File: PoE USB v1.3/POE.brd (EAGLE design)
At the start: 70.6 x 58.3 mm, 20 parts, among them X1 RJ45-6L21-B, X2 RJ45-6L21-B

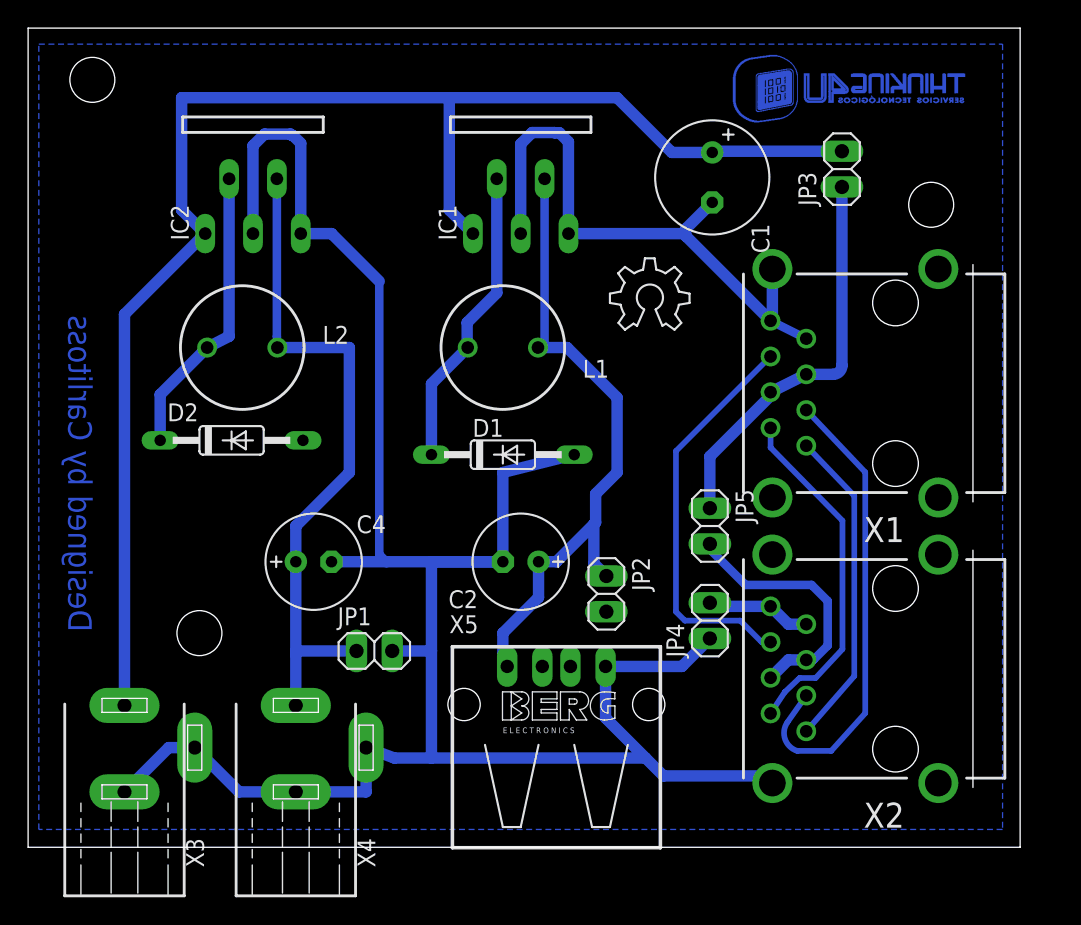
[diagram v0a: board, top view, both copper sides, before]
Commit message: PoE Modular acabado
Acabada la extracción o inyección de Power
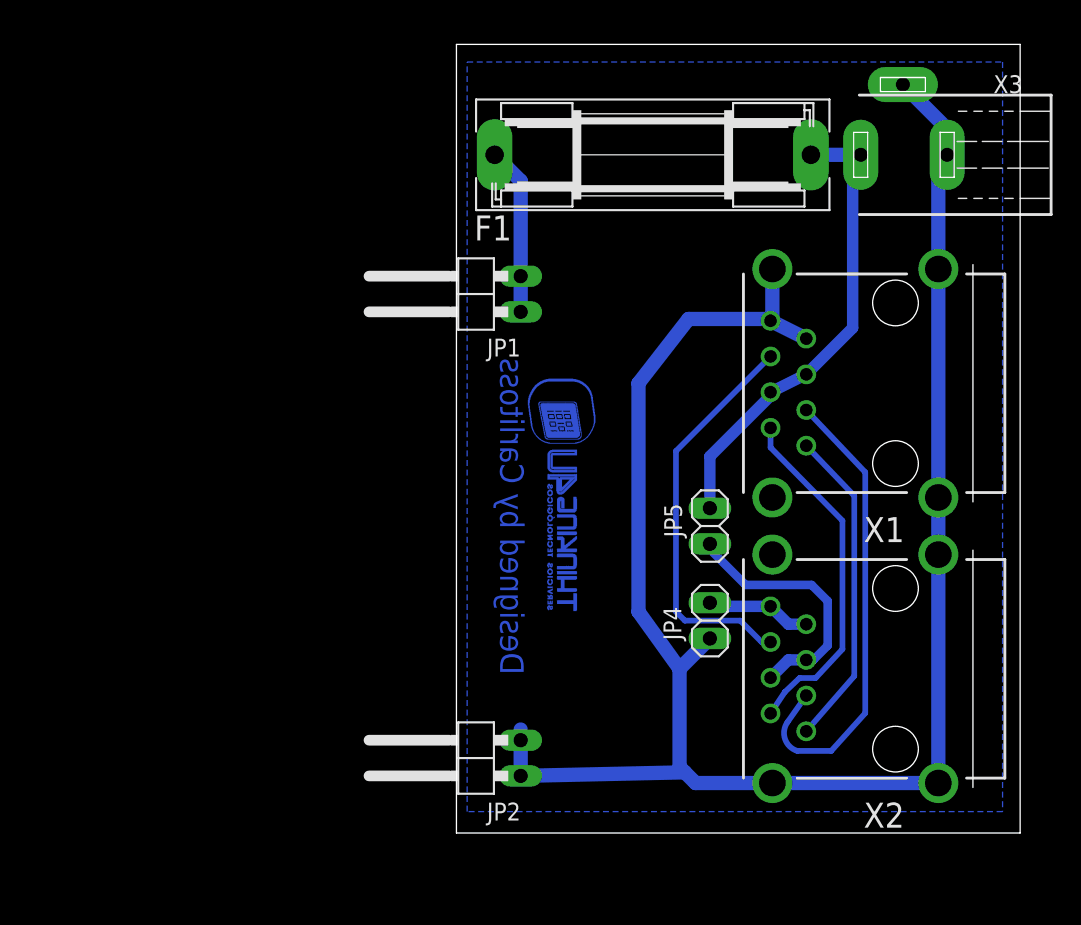
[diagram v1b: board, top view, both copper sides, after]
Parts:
- removed C1: 470uF, rcl:E3,5-8
- removed C2, C4: 220uF, rcl:E2,5-7
- removed D1, D2: 1N5824, diode:DO35-10
- removed IC1, IC2: (no value), linear:TO220-51
- removed JP3: (no value), pinhead:1X02
- removed L1, L2: 33uH, rcl:6000-XXXX-RC
- removed LOGO1: OSHW_LOGO_6MILX0200-NT, ohw-logo:OSHW_6X200_NOTEXT
- removed X4: (no value), con-conrad:733980-62
- removed X5: (no value), con-berg:PN87520
- added F1: (no value), fuse:SH22,5
- JP1, JP2: device pinhead:1X02 -> pinhead:1X02/90
- moved X3 77.4 mm to (158.5, 102.6), turned to 90 degrees
- moved JP1 26.2 mm to (121.9, 92.7), turned to 90 degrees
- moved JP2 15.3 mm to (121.9, 59.7), turned to 90 degrees
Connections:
- removed net N$2: C2.+, IC1.4, JP2.1, L1.2, X5.1
- removed net N$4: D2.C, IC2.2, L2.1
- removed net N$5: C4.+, IC2.4, JP1.1, L2.2, X4.1
- removed net VCC: C1.+, IC1.1, IC2.1, JP3.2, X3.1
- net GND: now also JP2.1; no longer C1.-, C2.-, C4.-, D1.A, D2.A, IC1.3, IC1.5, IC2.3, IC2.5, JP1.2, X4.2, X4.3, X5.4
- net N$1: now also F1.1, JP1.1, JP1.2; no longer D1.C, IC1.2, L1.1
- net N$9: now also F1.2, X3.1; no longer JP3.1
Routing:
- net VCC: track 105.3 -> 0.00 mm
- net GND: track 201.3 -> 135.0 mm
- net N$5: track 48.5 -> 0.00 mm
- net N$2: track 47.0 -> 0.00 mm
- net N$4: track 21.0 -> 0.00 mm
- net N$1: track 21.6 -> 11.9 mm
- net N$9: track 28.4 -> 34.0 mm
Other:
- board size 70.6 x 58.3 mm -> 40.1 x 56.1 mm
